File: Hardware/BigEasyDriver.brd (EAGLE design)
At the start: 36.8 x 30.5 mm, 53 parts, among them IC1 A4983ALT1, IC2 LM317L

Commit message: Started v15 revisions
Changed caps and resis to 0603, updated version number on PCB and
Schematic, re-routed a few traces.  Nowhere near done
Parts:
- C1, C10, C11, C2, C6, C7, C8, C9: device SparkFun:0402-CAP -> SparkFun:0603-CAP
- R1, R10, R11, R12, R13, R2, R20, R3, R4, R5, R6, R7, R8, R9: device SparkFun:0402-RES -> SparkFun:0603-RES
- moved R7 0.89 mm to (1.65, 22.9)
- moved C7 0.38 mm to (22.9, 9.27)
- moved R11 0.38 mm to (27.9, 9.27)
- moved R12 0.38 mm to (25.4, 9.27)
- moved R4 0.38 mm to (20.3, 9.27)
- moved R6 0.25 mm to (5.33, 22.9)
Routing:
- net N$4: track 3.94 -> 5.48 mm
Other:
- board text added: "v15"
- board text removed: "v14"

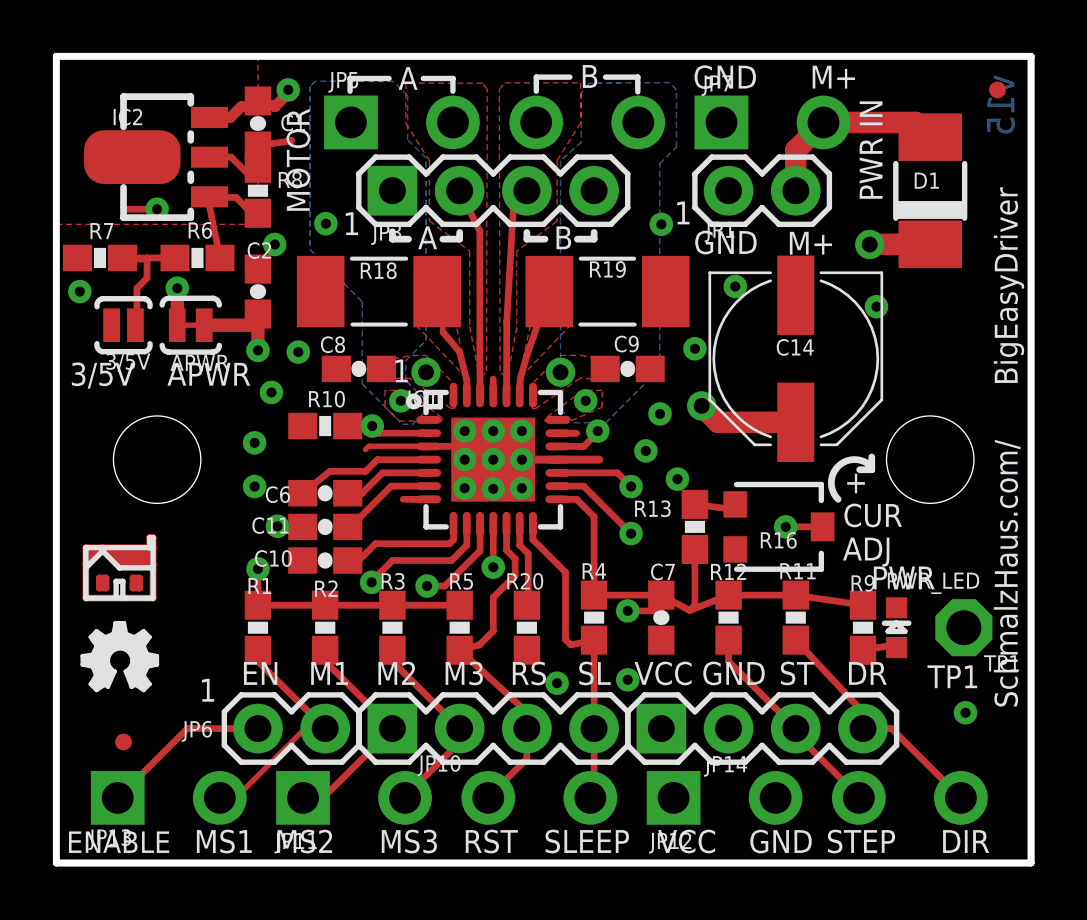
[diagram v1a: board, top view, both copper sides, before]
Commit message: Trace Re-Routes and Mask Changes
After changing caps/res to 0603 major re-routing happened.  Also changed
the mask settings to make sure the bigger vias were not covered.
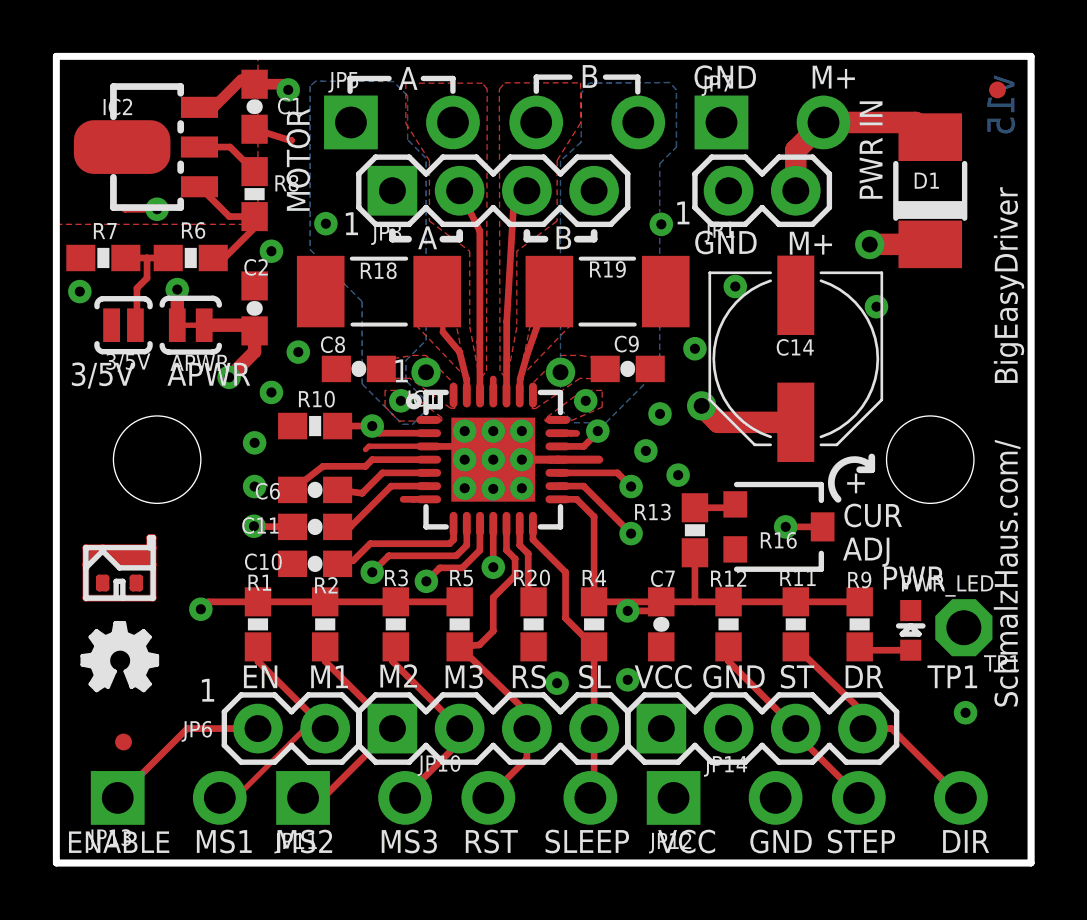
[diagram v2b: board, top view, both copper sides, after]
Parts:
- moved C2 0.65 mm to (7.49, 21.0)
- moved C1 0.65 mm to (7.49, 28.6)
- moved PWR_LED 0.54 mm to (32.3, 8.79)
- moved IC2 0.54 mm to (3.43, 27.1)
- moved C10 0.40 mm to (9.78, 11.3)
- moved C6 0.40 mm to (9.78, 14.1)
- moved C11 0.38 mm to (9.78, 12.7)
- moved R10 0.38 mm to (9.78, 16.5)
- moved R20 0.28 mm to (18.0, 9.02)
- moved C7 0.25 mm to (22.9, 9.02)
- moved R11 0.25 mm to (27.9, 9.02)
- moved R12 0.25 mm to (25.4, 9.02)
- moved R4 0.25 mm to (20.3, 9.02)
- moved R6 0.25 mm to (5.08, 22.9)
- moved R3 0.18 mm to (12.8, 9.02)
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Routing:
- net V+: track 57.6 -> 58.8 mm
- net N$4: track 5.48 -> 4.36 mm
- net VCC: track 31.7 -> 32.6 mm
- net SLEEP: track 12.1 -> 11.4 mm
- net N$2: track 1.33 -> 1.98 mm
- net 5V_ALT: track 8.13 -> 8.74 mm
- net N$6: track 4.43 -> 5.01 mm

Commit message: Trace cleanup
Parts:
- moved C6 0.13 mm to (9.78, 14.2)
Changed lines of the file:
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@@
 <layer number="27" name="tValues" color="7" fill="1" visible="no" active="yes"/>
 <layer number="28" name="bValues" color="7" fill="1" visible="no" active="yes"/>
-<layer number="29" name="tStop" color="7" fill="3" visible="yes" active="yes"/>
+<layer number="29" name="tStop" color="7" fill="3" visible="no" active="yes"/>
 <layer number="30" name="bStop" color="7" fill="6" visible="no" active="yes"/>
 <layer number="31" name="tCream" color="7" fill="4" visible="no" active="yes"/>
@@
 <layer number="13" name="Route13" color="4" fill="5" visible="no" active="no"/>
 <layer number="14" name="Route14" color="1" fill="6" visible="no" active="no"/>
-<layer number="15" name="GND" color="13" fill="1" visible="yes" active="yes"/>
-<layer number="2" name="VCC" color="14" fill="1" visible="yes" active="yes"/>
+<layer number="15" name="GND" color="13" fill="1" visible="no" active="yes"/>
+<layer number="2" name="VCC" color="14" fill="1" visible="no" active="yes"/>
 <layer number="3" name="Route3" color="4" fill="3" visible="no" active="no"/>
 <layer number="4" name="Route4" color="1" fill="4" visible="no" active="no"/>
@@
 </class>
 </classes>
-<designrules name="SparkFun *">
+<designrules name="SparkFun">
 <description language="en">&lt;b&gt;EAGLE Design Rules&lt;/b&gt;
 &lt;p&gt;
@@
 <param name="mlMinCreamFrame" value="0mil"/>
 <param name="mlMaxCreamFrame" value="0mil"/>
-<param name="mlViaStopLimit" value="24mil"/>
+<param name="mlViaStopLimit" value="20mil"/>
 <param name="srRoundness" value="0"/>
 <param name="srMinRoundness" value="0mil"/>
@@
 <attribute name="VALUE" x="17.2466" y="6.8834" size="0.6096" layer="27"/>
 </element>
-<element name="C6" library="SparkFun" package="0603-CAP" value=".1uf" x="9.779" y="14.097" smashed="yes">
-<attribute name="NAME" x="7.493" y="13.7414" size="0.6096" layer="25" font="vector"/>
-<attribute name="VALUE" x="11.0236" y="13.8684" size="0.6096" layer="27" font="vector"/>
+<element name="C6" library="SparkFun" package="0603-CAP" value=".1uf" x="9.779" y="14.224" smashed="yes">
+<attribute name="NAME" x="7.493" y="13.8684" size="0.6096" layer="25" font="vector"/>
+<attribute name="VALUE" x="11.0236" y="13.9954" size="0.6096" layer="27" font="vector"/>
 </element>
 <element name="C7" library="SparkFun" package="0603-CAP" value=".1uf" x="22.86" y="9.017" smashed="yes" rot="R270">
@@
 <wire x1="15.3035" y1="15.367" x2="15.4305" y2="15.24" width="0.254" layer="1"/>
 <wire x1="11.811" y1="15.748" x2="15.3035" y2="15.748" width="0.2032" layer="1"/>
-<wire x1="11.684" y1="15.621" x2="11.811" y2="15.748" width="0.2032" layer="1"/>
 <via x="15.4305" y="16.3195" extent="1-16" drill="0.381"/>
 <via x="16.51" y="16.3195" extent="1-16" drill="0.381"/>
@@
 <wire x1="16.51" y1="8.763" x2="16.51" y2="10.033" width="0.254" layer="1"/>
 <wire x1="15.987" y1="8.24" x2="16.51" y2="8.763" width="0.254" layer="1"/>
-<wire x1="15.24" y1="8.167" x2="15.987" y2="8.24" width="0.254" layer="1"/>
 <wire x1="17.78" y1="5.08" x2="17.78" y2="5.7" width="0.254" layer="1"/>
 <wire x1="17.78" y1="5.7" x2="15.24" y2="8.167" width="0.254" layer="1"/>
+<wire x1="15.987" y1="8.24" x2="15.313" y2="8.24" width="0.254" layer="1"/>
+<wire x1="15.313" y1="8.24" x2="15.24" y2="8.167" width="0.254" layer="1"/>
 </signal>
 <signal name="STEP">
@@
 <contactref element="IC1" pad="P$4"/>
 <contactref element="C6" pad="1"/>
-<wire x1="11.938" y1="15.24" x2="14.0701" y2="15.24" width="0.254" layer="1"/>
-<wire x1="11.938" y1="15.24" x2="11.684" y2="14.986" width="0.254" layer="1"/>
-<wire x1="11.684" y1="14.986" x2="10.072" y2="14.986" width="0.254" layer="1"/>
-<wire x1="10.072" y1="14.986" x2="8.929" y2="14.097" width="0.254" layer="1"/>
+<wire x1="14.0701" y1="15.24" x2="9.945" y2="15.24" width="0.254" layer="1"/>
+<wire x1="9.945" y1="15.24" x2="8.929" y2="14.224" width="0.254" layer="1"/>
 </signal>
 <signal name="N$9">
 <contactref element="IC1" pad="P$5"/>
 <contactref element="C6" pad="2"/>
-<wire x1="12.327" y1="14.74" x2="14.0702" y2="14.74" width="0.254" layer="1"/>
-<wire x1="11.557" y1="13.97" x2="12.327" y2="14.74" width="0.254" layer="1"/>
-<wire x1="10.629" y1="14.097" x2="11.557" y2="13.97" width="0.254" layer="1"/>
+<wire x1="14.0702" y1="14.74" x2="11.145" y2="14.74" width="0.254" layer="1"/>
+<wire x1="11.145" y1="14.74" x2="10.629" y2="14.224" width="0.254" layer="1"/>
 </signal>
 <signal name="N$19">

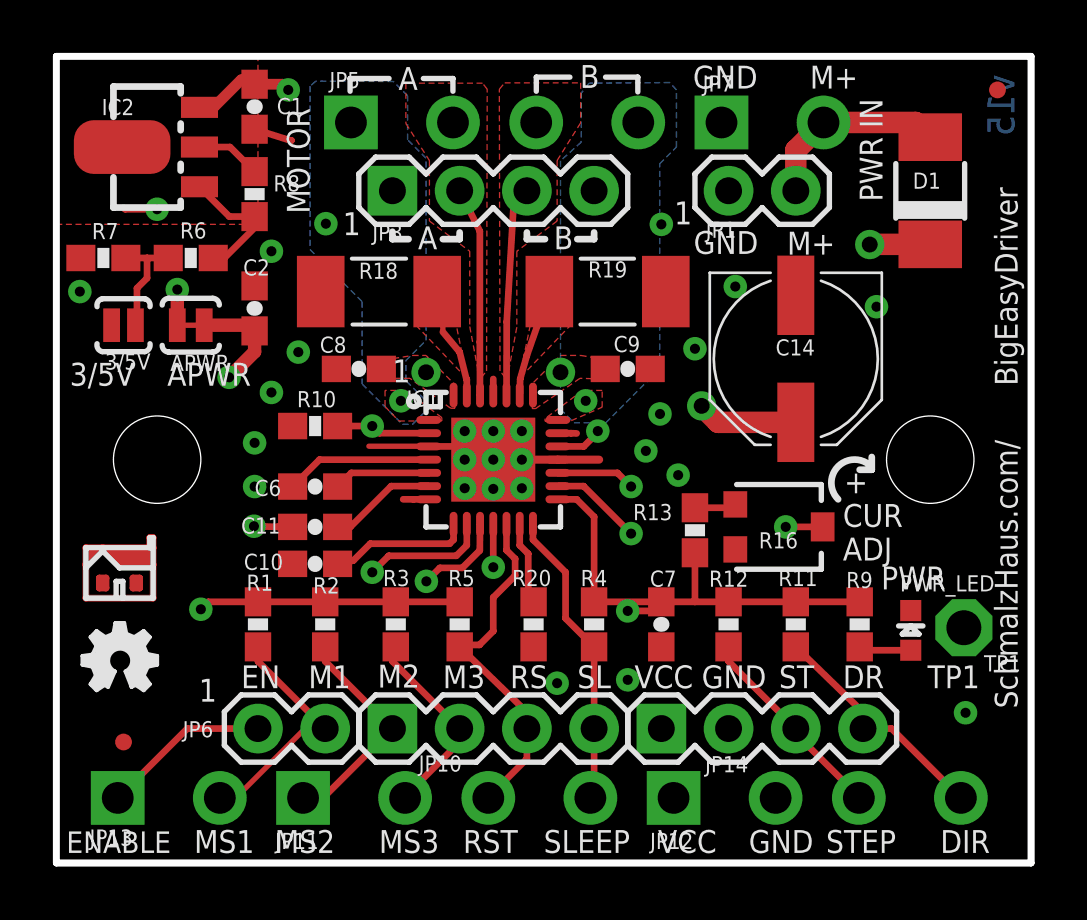
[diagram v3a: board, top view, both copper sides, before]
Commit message: Revised PLewis's Suggestions
Spaced the resistors to combat jumpers, revised a few trace angles.
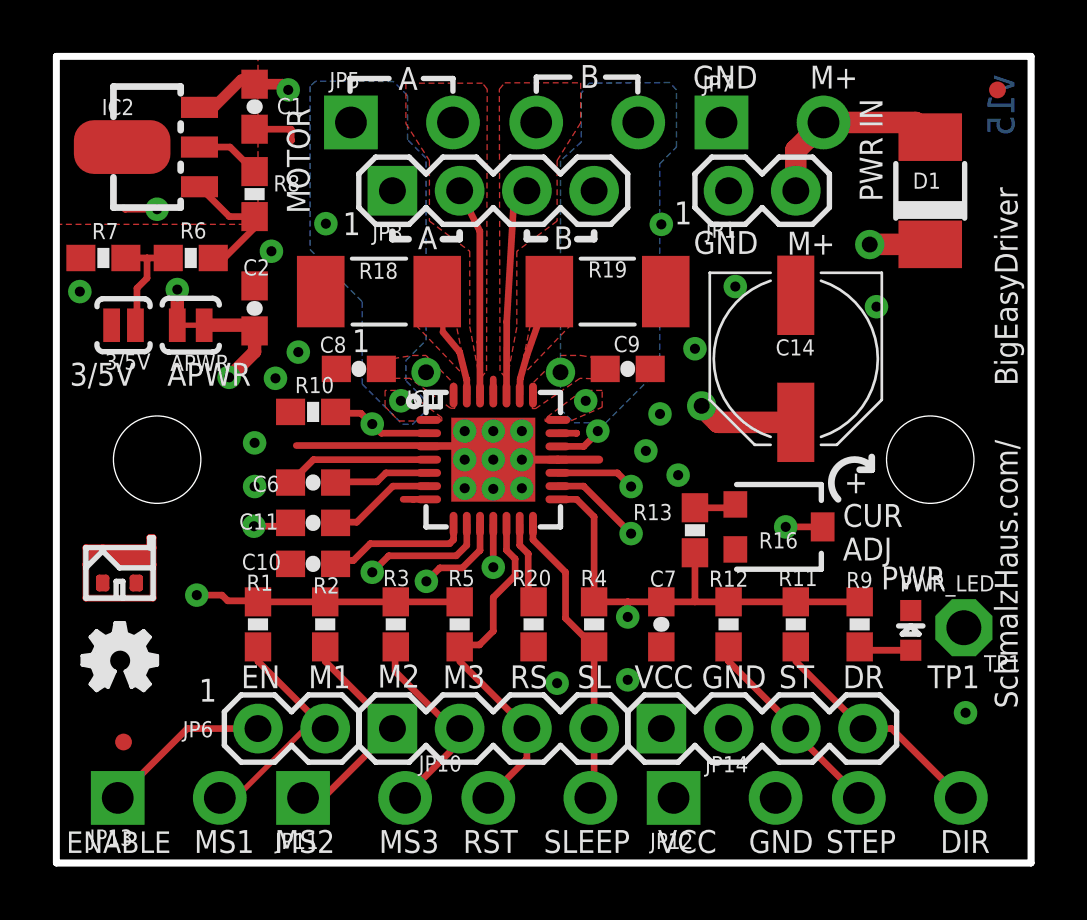
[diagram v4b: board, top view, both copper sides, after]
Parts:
- moved R10 0.54 mm to (9.70, 17.0)
- moved C11 0.17 mm to (9.70, 12.9)
- moved C6 0.17 mm to (9.70, 14.4)
- moved C10 0.08 mm to (9.70, 11.3)
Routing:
- net GND: track 9.68 -> 12.8 mm

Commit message: Drc Angle Check
Fixed as many DRC angle checks as possible.
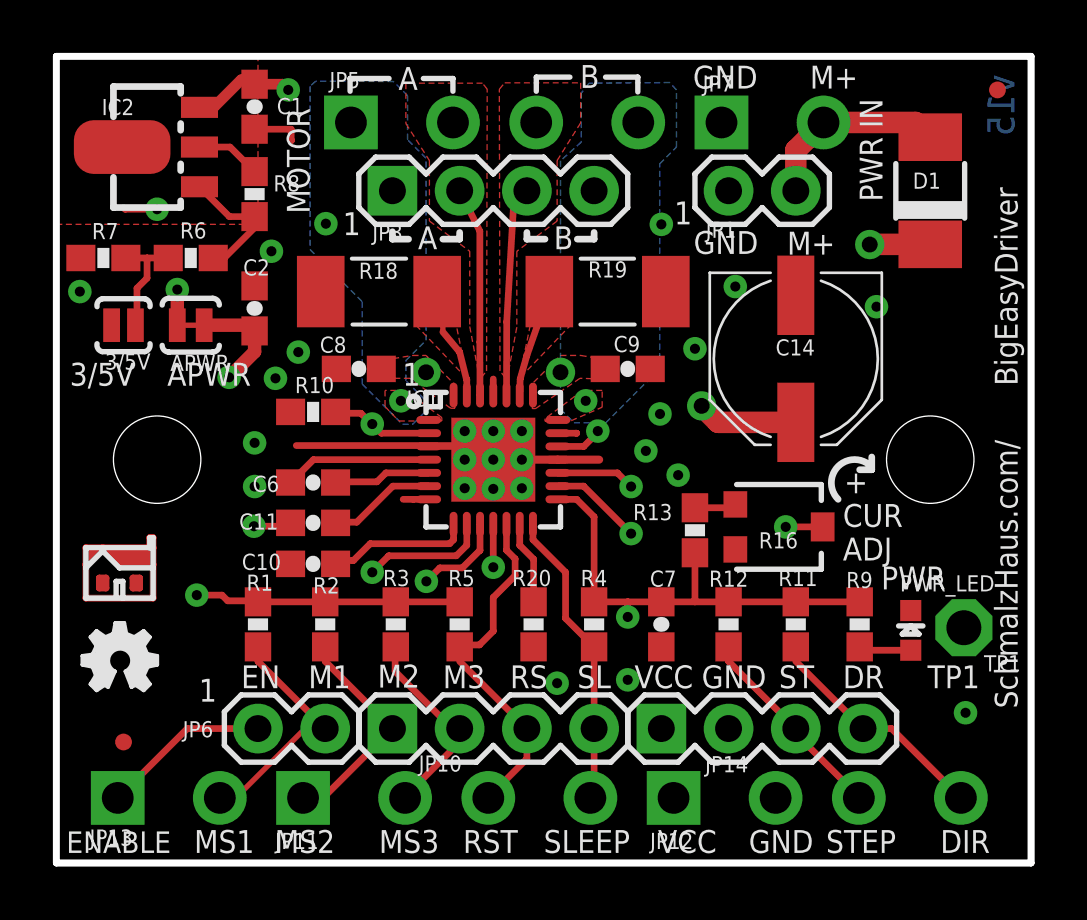
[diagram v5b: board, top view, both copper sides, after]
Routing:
- net VCC: track 32.7 -> 31.8 mm
- net N$19: track 3.69 -> 3.15 mm
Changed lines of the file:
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@@
 <setting verticaltext="up"/>
 </settings>
-<grid distance="0.05" unitdist="inch" unit="inch" style="lines" multiple="1" display="yes" altdistance="0.003" altunitdist="inch" altunit="inch"/>
+<grid distance="0.05" unitdist="inch" unit="inch" style="lines" multiple="1" display="yes" altdistance="0.005" altunitdist="inch" altunit="inch"/>
 <layers>
 <layer number="1" name="Top" color="4" fill="1" visible="yes" active="yes"/>
@@
 <layer number="13" name="Route13" color="4" fill="5" visible="no" active="no"/>
 <layer number="14" name="Route14" color="1" fill="6" visible="no" active="no"/>
-<layer number="15" name="GND" color="13" fill="1" visible="no" active="yes"/>
-<layer number="2" name="VCC" color="14" fill="1" visible="no" active="yes"/>
+<layer number="15" name="GND" color="13" fill="1" visible="yes" active="yes"/>
+<layer number="2" name="VCC" color="14" fill="1" visible="yes" active="yes"/>
 <layer number="3" name="Route3" color="4" fill="3" visible="no" active="no"/>
 <layer number="4" name="Route4" color="1" fill="4" visible="no" active="no"/>
@@
 <text x="36.322" y="5.842" size="0.8636" layer="21" font="vector" ratio="16" rot="R90">SchmalzHaus.com/</text>
 <text x="0.508" y="18.034" size="0.8636" layer="21" ratio="16">3/5V</text>
-<text x="11.176" y="19.304" size="0.8636" layer="21" font="vector" ratio="16">1</text>
+<text x="13.081" y="18.034" size="0.8636" layer="21" font="vector" ratio="16">1</text>
 <text x="29.718" y="12.7" size="0.8636" layer="21" font="vector" ratio="16">CUR</text>
 <text x="31.75" y="19.05" size="1.016" layer="2" font="vector" ratio="18">VCC</text>
@@
 <param name="mlMinCreamFrame" value="0mil"/>
 <param name="mlMaxCreamFrame" value="0mil"/>
-<param name="mlViaStopLimit" value="20mil"/>
+<param name="mlViaStopLimit" value="24mil"/>
 <param name="srRoundness" value="0"/>
 <param name="srMinRoundness" value="0mil"/>
@@
 <wire x1="6.477" y1="9.906" x2="7.581" y2="9.906" width="0.254" layer="1"/>
 <wire x1="7.581" y1="9.906" x2="7.62" y2="9.867" width="0.254" layer="1"/>
-<wire x1="22.86" y1="9.867" x2="22.86" y2="10.16" width="0.254" layer="1"/>
-<wire x1="22.845" y1="9.525" x2="22.86" y2="10.16" width="0.254" layer="1"/>
 </signal>
 <signal name="V+">
@@
 <contactref element="R20" pad="1"/>
 <wire x1="17.51" y1="12.0048" x2="17.51" y2="12.8001" width="0.254" layer="1"/>
-<wire x1="17.8308" y1="11.684" x2="17.51" y2="12.0048" width="0.254" layer="1"/>
-<wire x1="17.8308" y1="9.5908" x2="17.8308" y2="11.684" width="0.254" layer="1"/>
-<wire x1="18.034" y1="9.867" x2="17.8308" y2="9.5908" width="0.254" layer="1"/>
+<wire x1="18.034" y1="11.4808" x2="17.51" y2="12.0048" width="0.254" layer="1"/>
+<wire x1="18.034" y1="11.4808" x2="18.034" y2="9.867" width="0.254" layer="1"/>
 </signal>
 <signal name="N$20">
